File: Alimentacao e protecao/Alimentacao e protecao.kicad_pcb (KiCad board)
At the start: 2 copper layers, 20 parts, among them J1 PinoCheckBateriaVcc, J2 PinoCheckBateriaGND, J3 8.4V_PlacaCentral, J4 GND_PlacaCentral, Q1 BC548, Q2 BC548, SW1 SW_ON/OFF

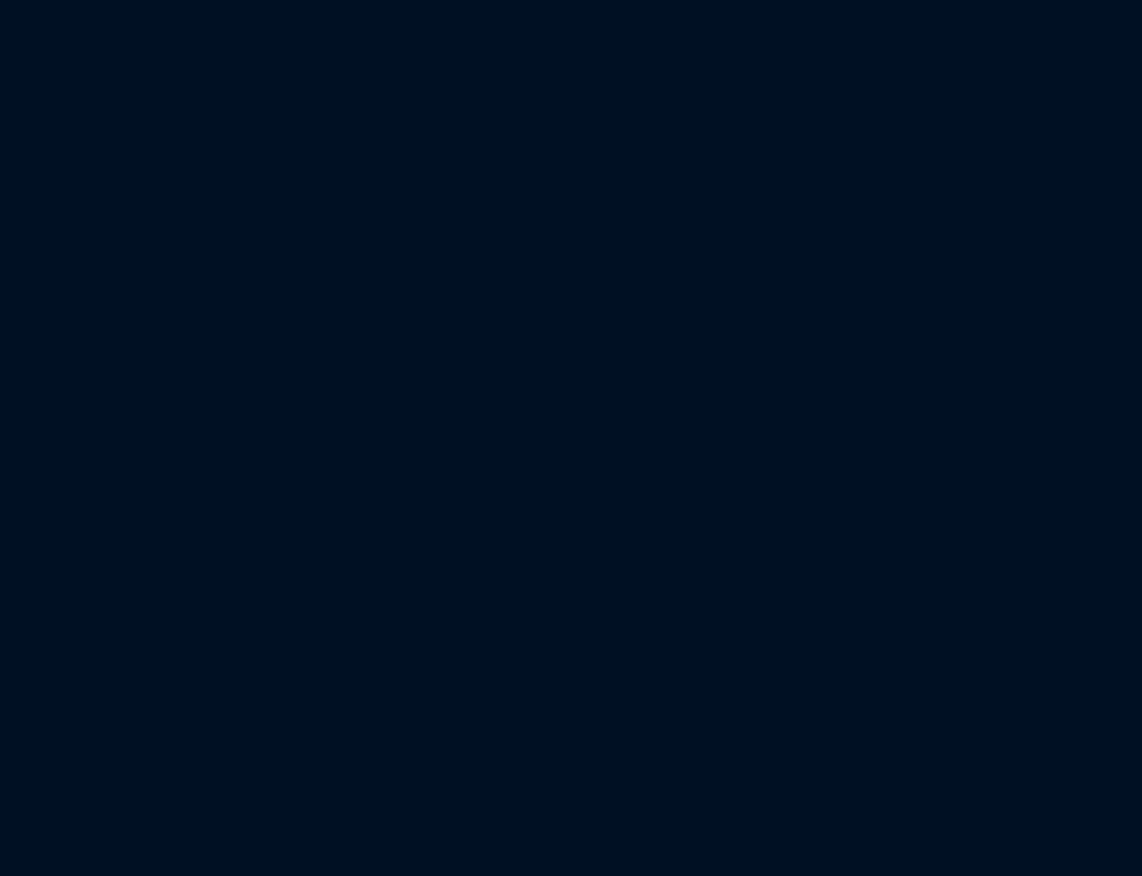
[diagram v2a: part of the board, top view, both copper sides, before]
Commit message: Criação pdf da placa de alimentação
Clearence de 0,8 mm
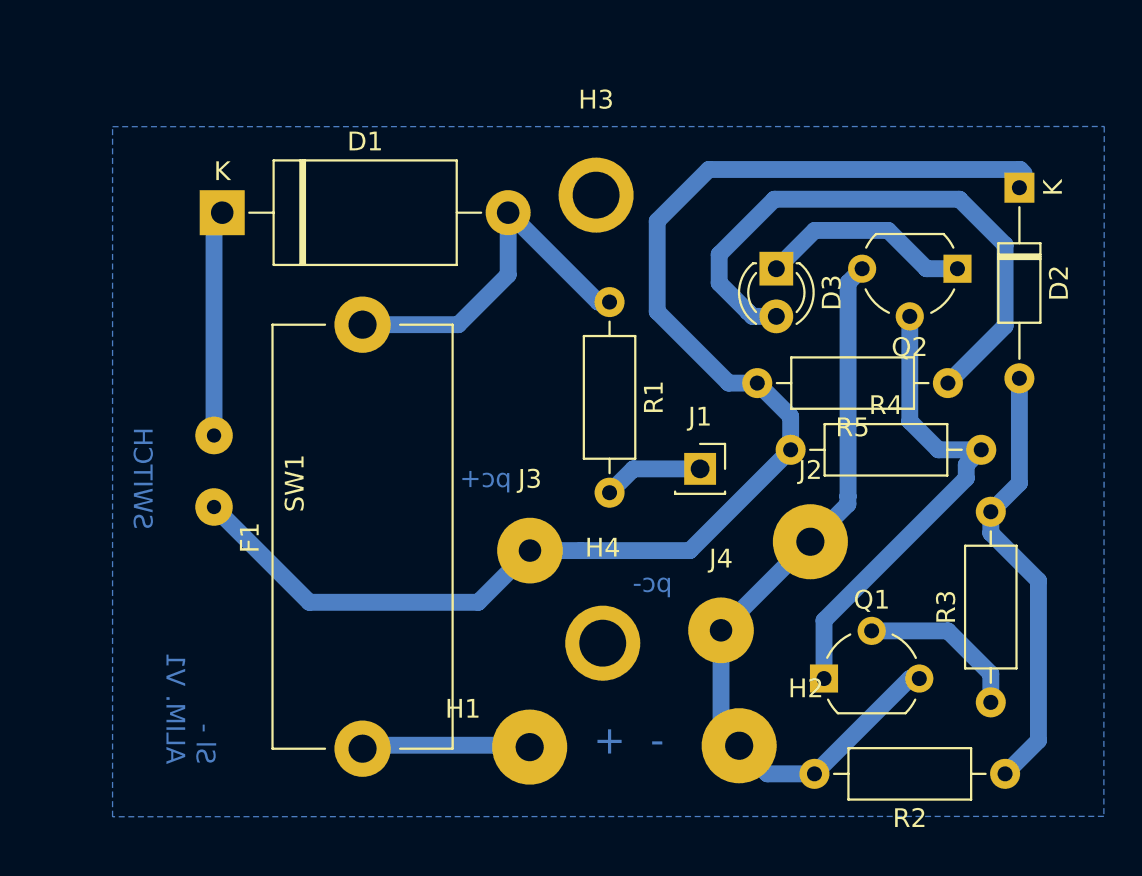
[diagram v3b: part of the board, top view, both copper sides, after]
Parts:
- added D1: DiodoProtecao-5A, Diode_THT:D_DO-27_P15.24mm_Horizontal, F.Cu at (205.2, 71.7)
- added D2: DiodoZener6.8V, Diode_THT:D_DO-35_SOD27_P10.16mm_Horizontal, F.Cu at (247.7, 70.4)
- added D3: LedBateriaVermelho, LED_THT:LED_D3.0mm, F.Cu at (234.7, 74.7)
- added F1: Fuse-5A, Fuse:Fuseholder_Cylinder-5x20mm_Stelvio-Kontek_PTF78_Horizontal_Open, F.Cu at (212.6, 100.3)
- added H1: V8.4 - Lipo, Connector_Wire:SolderWirePad_1x01_Drill1.5mm, F.Cu at (221.5, 100.2)
- added H2: GND - Lipo, Connector_Wire:SolderWirePad_1x01_Drill1.5mm, F.Cu at (232.7, 100.1)
- added H3: Furos, Wire_Pads:SolderWirePad_single_2-5mmDrill, F.Cu at (225.1, 70.8)
- added H4: Furos, Wire_Pads:SolderWirePad_single_2-5mmDrill, F.Cu at (225.4, 94.6)
- added J1: PinoCheckBateriaVcc, Connector_PinSocket_2.54mm:PinSocket_1x01_P2.54mm_Vertical, F.Cu at (230.6, 85.3)
- added J2: PinoCheckBateriaGND, Connector_Wire:SolderWirePad_1x01_Drill1.5mm, F.Cu at (236.5, 89.2)
- added J3: 8.4V_PlacaCentral, Connector_Wire:SolderWirePad_1x01_Drill1.2mm, F.Cu at (221.6, 89.7)
- added J4: GND_PlacaCentral, Connector_Wire:SolderWirePad_1x01_Drill1.2mm, F.Cu at (231.7, 93.9)
- added Q1: BC548, Package_TO_SOT_THT:TO-92_Wide, F.Cu at (237.2, 96.5)
- added Q2: BC548, Package_TO_SOT_THT:TO-92_Wide, F.Cu at (244.3, 74.7)
- added R1: RBatCheck10K, Resistor_THT:R_Axial_DIN0207_L6.3mm_D2.5mm_P10.16mm_Horizontal, F.Cu at (225.8, 76.5)
- added R2: R6K6MedidorDeBateria, Resistor_THT:R_Axial_DIN0207_L6.3mm_D2.5mm_P10.16mm_Horizontal, F.Cu at (246.9, 101.6)
- added R3: R1KMedidorDeBateria, Resistor_THT:R_Axial_DIN0207_L6.3mm_D2.5mm_P10.16mm_Horizontal, F.Cu at (246.1, 97.8)
- added R4: R10KMedidorDeBateria, Resistor_THT:R_Axial_DIN0207_L6.3mm_D2.5mm_P10.16mm_Horizontal, F.Cu at (235.5, 84.3)
- added R5: RMedidorDeBateria1K, Resistor_THT:R_Axial_DIN0207_L6.3mm_D2.5mm_P10.16mm_Horizontal, F.Cu at (243.8, 80.8)
- added SW1: SW_ON/OFF, CUSTOM_Placa_central_v01:Solder_Pad_Custom, F.Cu at (208.5, 86.1)
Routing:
- net 8.4V: track 73.0 -> 146.0 mm
- net GND: track 41.7 -> 83.4 mm
- net Net-(D3-Pad2): track 31.4 -> 62.8 mm
- net Net-(Q1-Pad1): track 25.7 -> 51.4 mm
- net Net-(D2-Pad2): track 23.5 -> 47.0 mm
- net Net-(D1-Pad2): track 19.6 -> 39.1 mm
- net Net-(D1-Pad1): track 12.1 -> 24.1 mm
- net Net-(D3-Pad1): track 11.3 -> 22.7 mm
- net Net-(F1-Pad1): track 9.02 -> 18.0 mm
- net Net-(Q1-Pad2): track 8.82 -> 17.6 mm
- net Net-(J1-Pad1): track 5.35 -> 10.7 mm

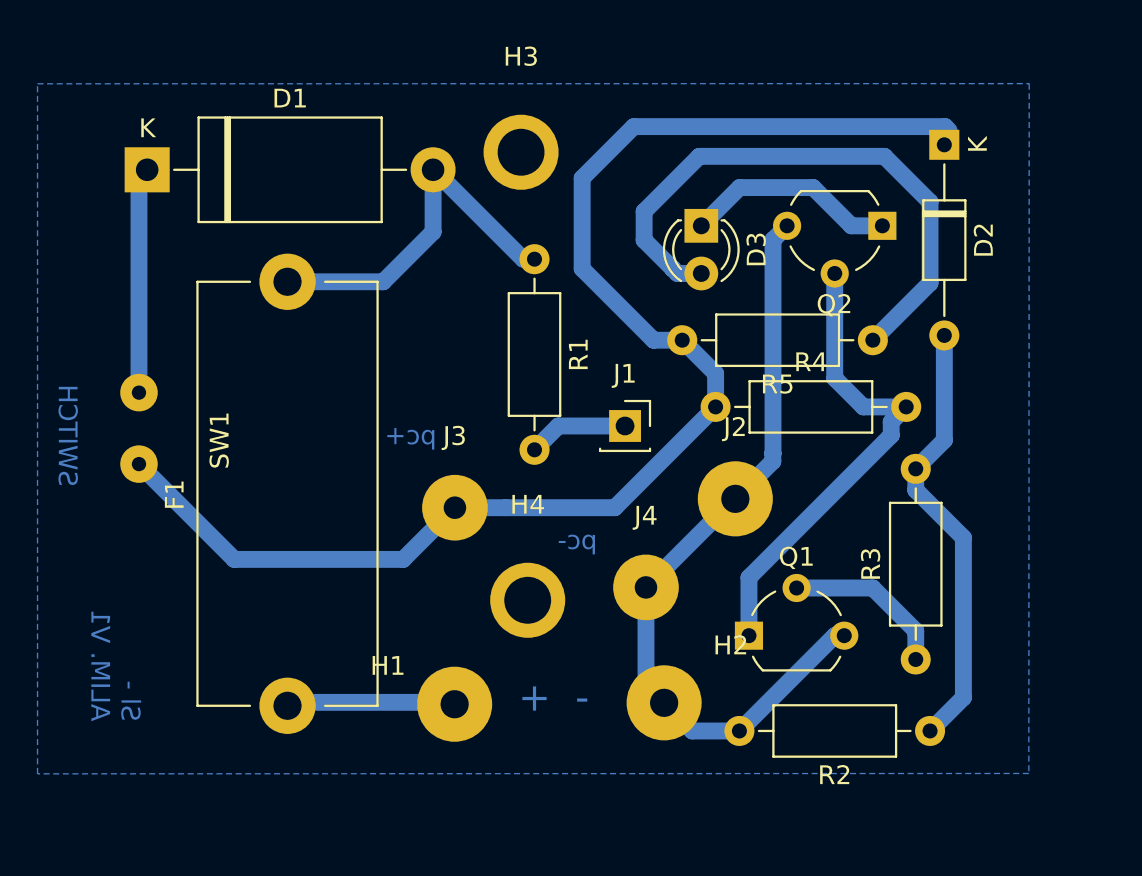
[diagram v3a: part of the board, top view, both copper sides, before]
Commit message: Correção nas pcbs
Nome da placa de encoder desinvertido
Trilhas laterais de GND da placa central mais espaçadas nos cantos
Nome da equipe colocado na placa central
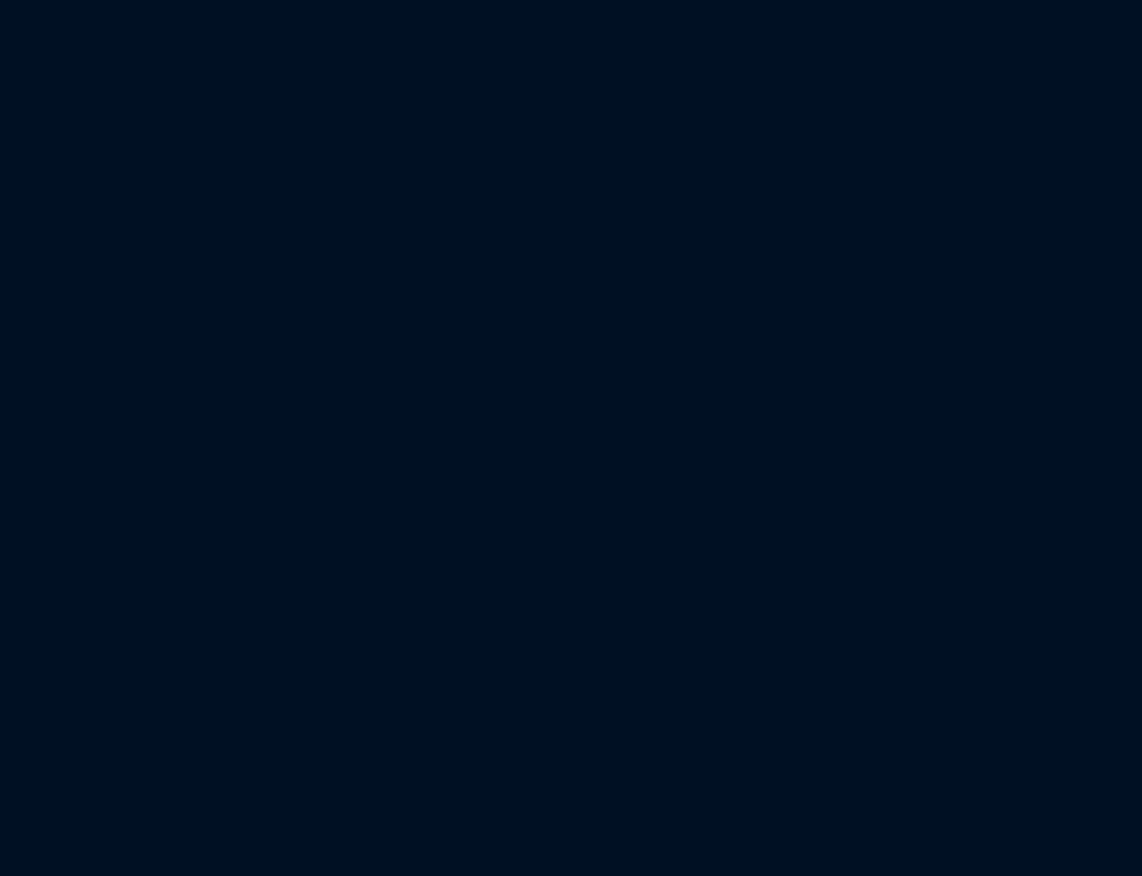
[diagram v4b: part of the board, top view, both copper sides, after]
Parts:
- removed the D1 at (58.1, 69.4)
- removed the D2 at (100.6, 68.1)
- removed the D3 at (87.6, 72.4)
- removed the F1 at (65.6, 98.0)
- removed the H1 at (74.5, 97.9)
- removed the H2 at (85.6, 97.8)
- removed the H3 at (78.0, 68.5)
- removed the H4 at (78.4, 92.3)
- removed the J1 at (83.6, 83.1)
- removed the J2 at (89.4, 86.9)
- removed the J3 at (74.5, 87.4)
- removed the J4 at (84.7, 91.7)
- removed the Q1 at (90.2, 94.2)
- removed the Q2 at (97.3, 72.4)
- removed the R1 at (78.7, 74.2)
- removed the R2 at (99.8, 99.3)
- removed the R3 at (99.1, 95.5)
- removed the R4 at (88.4, 82.0)
- removed the R5 at (96.8, 78.5)
- removed the SW1 at (61.5, 83.8)
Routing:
- net 8.4V: track 146.0 -> 73.0 mm
- net GND: track 83.4 -> 41.7 mm
- net Net-(D3-Pad2): track 62.8 -> 31.4 mm
- net Net-(Q1-Pad1): track 51.4 -> 25.7 mm
- net Net-(D2-Pad2): track 47.0 -> 23.5 mm
- net Net-(D1-Pad2): track 39.1 -> 19.6 mm
- net Net-(D1-Pad1): track 24.1 -> 12.1 mm
- net Net-(D3-Pad1): track 22.7 -> 11.3 mm
- net Net-(F1-Pad1): track 18.0 -> 9.02 mm
- net Net-(Q1-Pad2): track 17.6 -> 8.82 mm
- net Net-(J1-Pad1): track 10.7 -> 5.35 mm

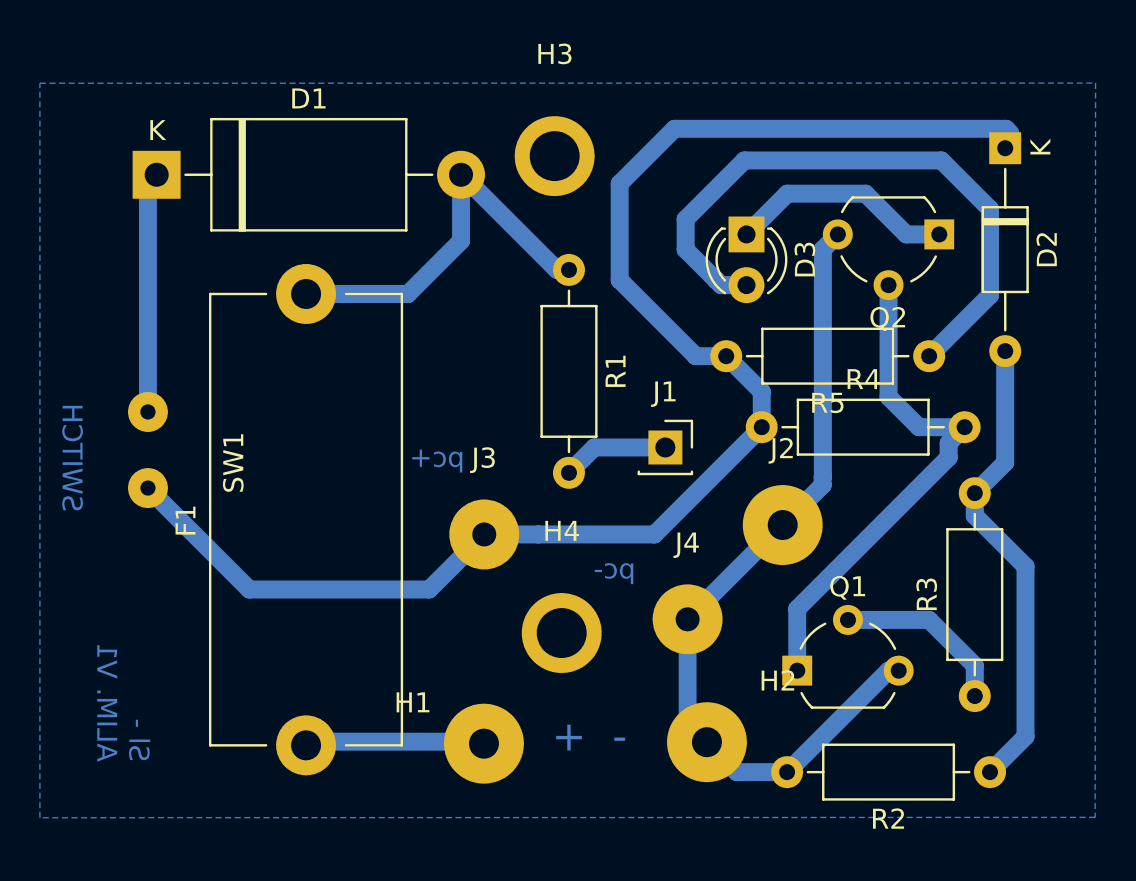
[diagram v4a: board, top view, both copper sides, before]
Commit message: Acertada as placas e os pdfs
Acertada as placas centrais, de alimentação e de conector.
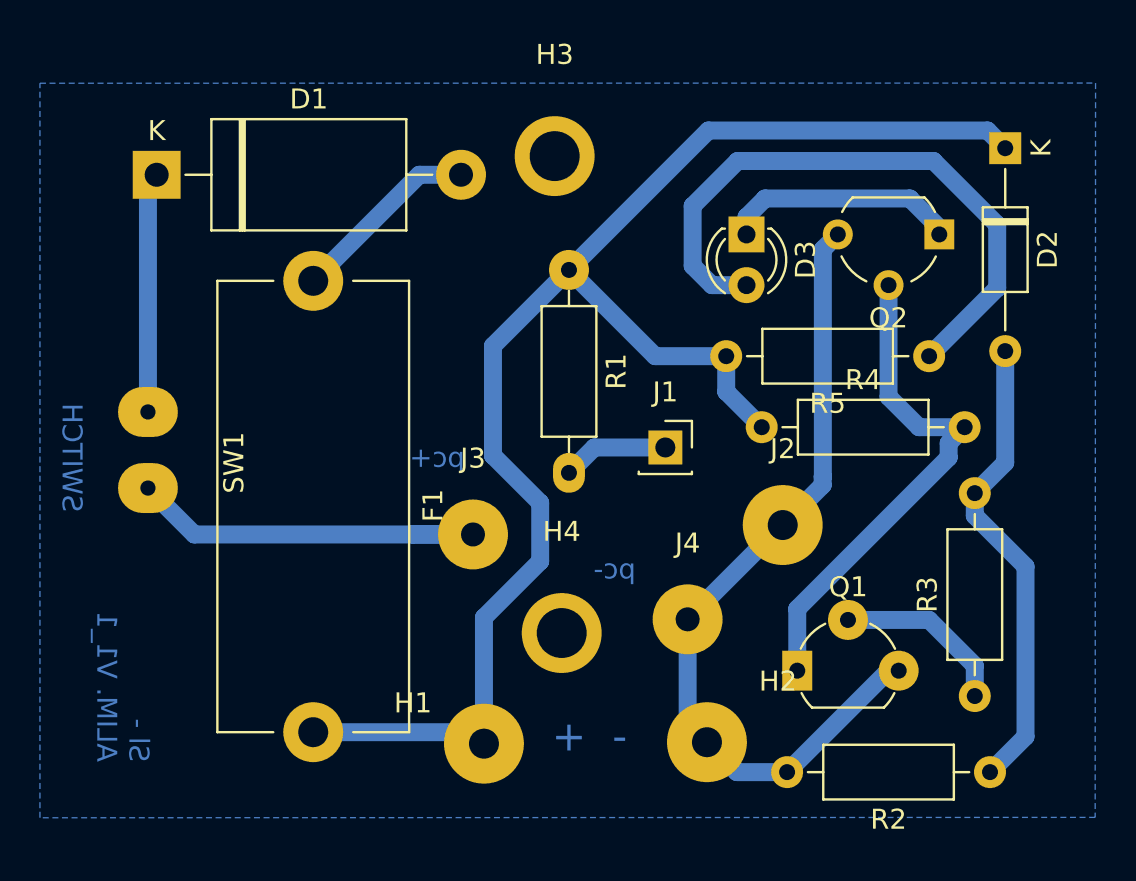
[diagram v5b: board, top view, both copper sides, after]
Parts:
- R1: value RBatCheck10K -> R10KBatCheck
- R5: value RMedidorDeBateria1K -> R1KMedidorDeBateria
- moved F1 23.3 mm to (213.0, 77.0), turned to 270 degrees
- moved J3 0.56 mm to (221.0, 89.7)
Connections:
- D2 pad 1: 8.4V -> 8.4VCircuitoMedidor
- F1 pad 1: Net-(F1-Pad1) -> Net-(D1-Pad2)
- F1 pad 2: Net-(D1-Pad2) -> 8.4VCircuitoMedidor
- H1 pad 1: Net-(F1-Pad1) -> 8.4VCircuitoMedidor
- J3 pad 1: 8.4V -> Net-(J3-Pad1)
- R1 pad 1: Net-(D1-Pad2) -> 8.4VCircuitoMedidor
- R4 pad 1: 8.4V -> 8.4VCircuitoMedidor
- R5 pad 2: 8.4V -> 8.4VCircuitoMedidor
- SW1 pad 1: 8.4V -> Net-(J3-Pad1)
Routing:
- net 8.4VCircuitoMedidor: track 0.00 -> 75.3 mm
- net 8.4V: track 73.0 -> 0.00 mm
- net Net-(J3-Pad1): track 0.00 -> 20.9 mm
- net Net-(D1-Pad2): track 19.6 -> 9.60 mm
- net Net-(F1-Pad1): track 9.02 -> 0.00 mm
- net Net-(D3-Pad1): track 11.3 -> 11.8 mm
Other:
- board text added: "Sl - ALIM. V1_1"
- board text removed: "Sl - ALIM. V1"
